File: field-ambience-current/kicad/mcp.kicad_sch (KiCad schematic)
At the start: 68 parts, among them SW10 Modifier CLEAR (12x12x7.3 SMD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, SW6 Modifier SHIFT (12x12x7.3 SMD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, SW7 Modifier HOLD (12x12x7.3 SMD-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, SW8 Modifier DRONE (12x12x7.3 SMD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, SW9 Modifier GENERATE (12x12x7.3 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, U10 PCA9685PW #2 (16-Ch I²C PWM, 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, U2 MCP23017-E/SS (I/O-Expander), U6 PCA9685PW (16-Ch I²C PWM LED-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

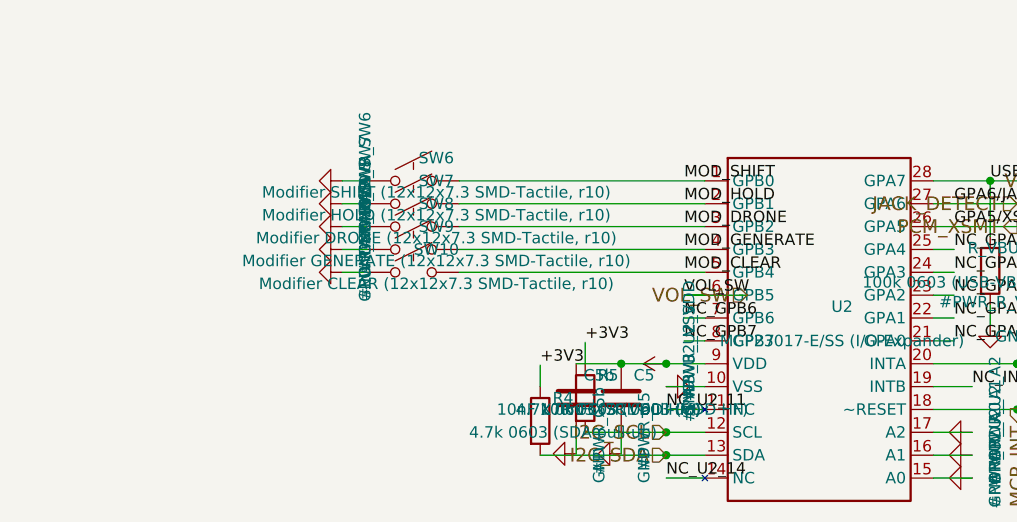
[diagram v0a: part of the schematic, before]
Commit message: parts: resolve ECO items — MIDI LCSC, button SMD→THT, TPS22918 LCSC, pinmap (#79)
* docs(pcb): completeness package — pinmap, JLC BOM export, handoff doc

Make the PCB design data component- and connectivity-complete so a PCB
engineer knows every pin / net / module without re-deriving from the
generator. Closes the gaps from the hardware gap analysis: the BOM alone
isn't production-ready, the generator is the source of truth, and the
pinmap / machine BOM / handoff package were missing.

New deliverables:
- docs/hardware/PINMAP.md — every STM32H743 LQFP-100 pin (all 100) → net →
  function/AF → module → external-component pin, plus per-module net tables
  (source → all sinks) for Power/MCU/LCD/MCP+LEDs/Encoders/Audio/Battery,
  and the verified free-pin list. Distilled from the generator NETS table.
- kicad/export_jlc_bom.py — stdlib-only JLC BOM exporter; parses the 7
  generated leaf .kicad_sch, skips #PWR + DNP, groups by LCSC, quotes
  comma-bearing values. Parts without LCSC go to a stderr NO-LCSC list
  (no guessing). Prints that CPL needs a routed .kicad_pcb (doesn't exist).
- kicad/jlc_bom.csv — generated: 57 LCSC parts, 188 placements.
- docs/hardware/PCB_HANDOFF.md — what's in the package, the engineer
  workflow, and the hard blockers before a fab order (ERC in GUI, layout +
  routing, mechanical coords, Gerber/CPL — all KiCad-GUI / user-side since
  there is no kicad-cli in this env).

Generator: swap LED6/LED7 physical colors to spec — Shift = gelb (C2287),
Hold = gruen (C12624) — attribute-only (same footprint/pads/net), so the
schematic, BOM and firmware are now consistent. Regenerated mcp.kicad_sch.

Also: PROJECT_STATUS r18.64 (1.9" display freeze, per-world musical
identity, Echo/Blur); MECHANICAL_REQUIREMENTS 1.9" freeze line;
component_reviews/README F-1/F-2/F-3 status corrections.

Docs/kicad/tools only — outside the firmware CI path filter.

Co-Authored-By: Claude Opus 4.8 <noreply@anthropic.com>
Claude-Session: https://claude.ai/code/session_01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
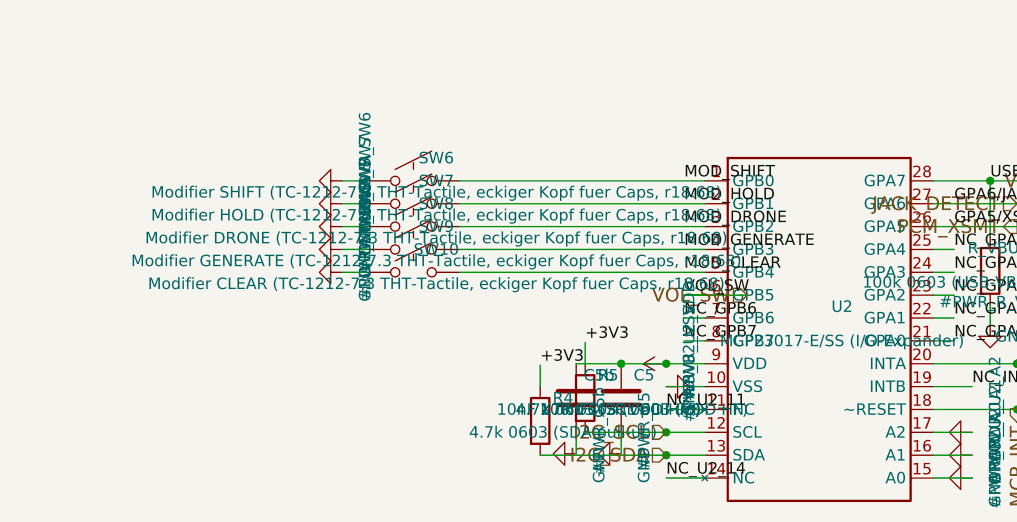
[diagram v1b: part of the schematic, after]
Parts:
- SW10: value Modifier CLEAR (12x12x7.3 SMD-Tactile, r10) -> Modifier CLEAR (TC-1212-7.3 THT-Tactile, eckiger Kopf fuer Caps, r18.68); footprint field_ambience:SW_HX_12x12x7.3_SMD-4P -> field_ambience:SW_TC1212-7.3_THT_4P; FP_NOTE Custom-Footprint libraries/field_ambience.pretty/SW_HX_12x1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 -> field_ambience:SW_TC1212-7.3_THT_4P (easyeda2kicad C2845240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; LCSC C36498966 -> C2845240; MPN HX 12x12x7.3TPFT-B -> TC-1212-7.3-260G; Manufacturer hanxia -> HCTL; Package SMD-4P 11.8x11.8mm, vertical tactile, 7.3mm height, SPST 25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 -> THT 4-pin 11.8x11.8mm, square-head plunger 7.3mm (clip-on c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
- SW6: value Modifier SHIFT (12x12x7.3 SMD-Tactile, r10) -> Modifier SHIFT (TC-1212-7.3 THT-Tactile, eckiger Kopf fuer Caps, r18.68); footprint field_ambience:SW_HX_12x12x7.3_SMD-4P -> field_ambience:SW_TC1212-7.3_THT_4P; FP_NOTE Custom-Footprint libraries/field_ambience.pretty/SW_HX_12x1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 -> field_ambience:SW_TC1212-7.3_THT_4P (easyeda2kicad C2845240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; LCSC C36498966 -> C2845240; MPN HX 12x12x7.3TPFT-B -> TC-1212-7.3-260G; Manufacturer hanxia -> HCTL; Package SMD-4P 11.8x11.8mm, vertical tactile, 7.3mm height, SPST 25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 -> THT 4-pin 11.8x11.8mm, square-head plunger 7.3mm (clip-on c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
- SW7: value Modifier HOLD (12x12x7.3 SMD-Tactile, r10) -> Modifier HOLD (TC-1212-7.3 THT-Tactile, eckiger Kopf fuer Caps, r18.68); footprint field_ambience:SW_HX_12x12x7.3_SMD-4P -> field_ambience:SW_TC1212-7.3_THT_4P; FP_NOTE Custom-Footprint libraries/field_ambience.pretty/SW_HX_12x1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 -> field_ambience:SW_TC1212-7.3_THT_4P (easyeda2kicad C2845240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; LCSC C36498966 -> C2845240; MPN HX 12x12x7.3TPFT-B -> TC-1212-7.3-260G; Manufacturer hanxia -> HCTL; Package SMD-4P 11.8x11.8mm, vertical tactile, 7.3mm height, SPST 25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 -> THT 4-pin 11.8x11.8mm, square-head plunger 7.3mm (clip-on c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
- SW8: value Modifier DRONE (12x12x7.3 SMD-Tactile, r10) -> Modifier DRONE (TC-1212-7.3 THT-Tactile, eckiger Kopf fuer Caps, r18.68); footprint field_ambience:SW_HX_12x12x7.3_SMD-4P -> field_ambience:SW_TC1212-7.3_THT_4P; FP_NOTE Custom-Footprint libraries/field_ambience.pretty/SW_HX_12x1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 -> field_ambience:SW_TC1212-7.3_THT_4P (easyeda2kicad C2845240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; LCSC C36498966 -> C2845240; MPN HX 12x12x7.3TPFT-B -> TC-1212-7.3-260G; Manufacturer hanxia -> HCTL; Package SMD-4P 11.8x11.8mm, vertical tactile, 7.3mm height, SPST 25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 -> THT 4-pin 11.8x11.8mm, square-head plunger 7.3mm (clip-on c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
- SW9: value Modifier GENERATE (12x12x7.3 SMD-Tactile, r10) -> Modifier GENERATE (TC-1212-7.3 THT-Tactile, eckiger Kopf fuer Caps, r18.68); footprint field_ambience:SW_HX_12x12x7.3_SMD-4P -> field_ambience:SW_TC1212-7.3_THT_4P; FP_NOTE Custom-Footprint libraries/field_ambience.pretty/SW_HX_12x1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 -> field_ambience:SW_TC1212-7.3_THT_4P (easyeda2kicad C2845240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; LCSC C36498966 -> C2845240; MPN HX 12x12x7.3TPFT-B -> TC-1212-7.3-260G; Manufacturer hanxia -> HCTL; Package SMD-4P 11.8x11.8mm, vertical tactile, 7.3mm height, SPST 25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 -> THT 4-pin 11.8x11.8mm, square-head plunger 7.3mm (clip-on c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

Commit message: kicad(gen): flow the 5 sourcing-fix part swaps into the generator (r18.71)
The generator is the schematic's source of truth, so the BOM part swaps must
live here (previously only in BOM/HTML). Swapped LCSC + MPN in the generator,
regenerated the .kicad_sch, re-exported jlc_bom.csv:
- FB2 ferrite C84094 -> C19330 (same Murata MPN, JLC 950k)
- VCAP C24539 -> C23630 (2.2uF 16V X5R 0603, JLC Basic)
- charger LED C72041 (blue+EOL!) -> C965800 (orange 605nm 0603)
- C_BULK2 C2880380 (stock 1) -> C23742 (100uF 10V X5R 1210)
- modifier buttons SW6-10 C2845240 (stock 30) -> C36498965 (HX B3F square
  head); footprint SW_TC1212-7.3_THT_4P reused, HX pinout verify noted in FP_NOTE.

The generated schematic Aron opens now carries the correct in-stock parts.
check_pinmap passes; jlc_bom.csv has the new codes (old ones gone).

Co-Authored-By: Claude Opus 4.8 <noreply@anthropic.com>
Claude-Session: https://claude.ai/code/session_01K5kLTFpDCCoYwx2dq6RkAv
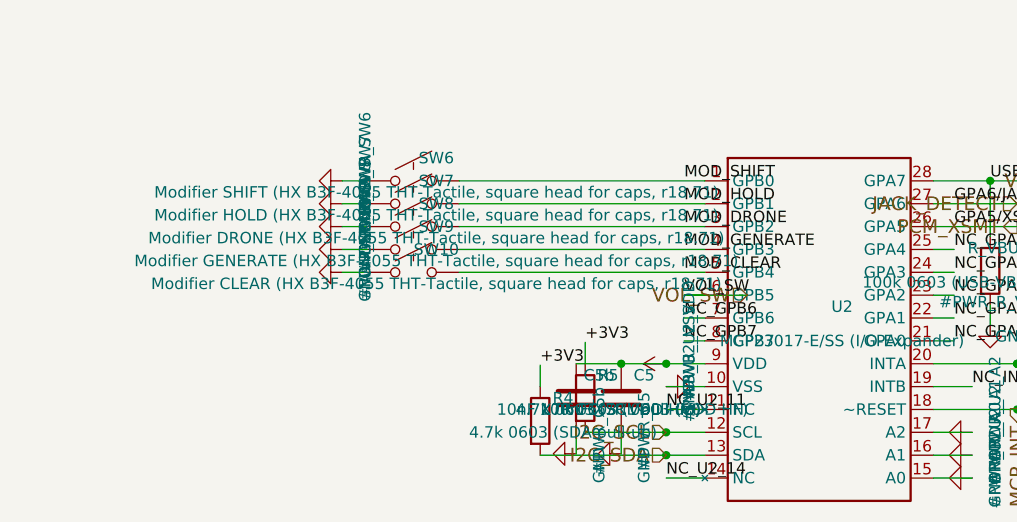
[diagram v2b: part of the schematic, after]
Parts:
- SW10: value Modifier CLEAR (TC-1212-7.3 THT-Tactile, eckiger Kopf fuer Caps, r18.68) -> Modifier CLEAR (HX B3F-4055 THT-Tactile, square head for caps, r18.71); FP_NOTE field_ambience:SW_TC1212-7.3_THT_4P (easyeda2kicad C2845240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 -> r18.71: was TC-1212-7.3-260G C2845240 (JLC stock 30); -> HX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; LCSC C2845240 -> C36498965; MPN TC-1212-7.3-260G -> HX B3F-4055-Y; Manufacturer HCTL -> HX; Package THT 4-pin 11.8x11.8mm, square-head plunger 7.3mm (clip-on caps), SPST 2.6N, 100k cycles, 12V/50mA -> THT 4-pin 11.8x11.8mm, square-head plunger 7.3mm (clip-on caps), SPST 2.5N, 100k cycles, 12V/50mA
- SW6: value Modifier SHIFT (TC-1212-7.3 THT-Tactile, eckiger Kopf fuer Caps, r18.68) -> Modifier SHIFT (HX B3F-4055 THT-Tactile, square head for caps, r18.71); FP_NOTE field_ambience:SW_TC1212-7.3_THT_4P (easyeda2kicad C2845240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 -> r18.71: was TC-1212-7.3-260G C2845240 (JLC stock 30); -> HX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; LCSC C2845240 -> C36498965; MPN TC-1212-7.3-260G -> HX B3F-4055-Y; Manufacturer HCTL -> HX; Package THT 4-pin 11.8x11.8mm, square-head plunger 7.3mm (clip-on caps), SPST 2.6N, 100k cycles, 12V/50mA -> THT 4-pin 11.8x11.8mm, square-head plunger 7.3mm (clip-on caps), SPST 2.5N, 100k cycles, 12V/50mA
- SW7: value Modifier HOLD (TC-1212-7.3 THT-Tactile, eckiger Kopf fuer Caps, r18.68) -> Modifier HOLD (HX B3F-4055 THT-Tactile, square head for caps, r18.71); FP_NOTE field_ambience:SW_TC1212-7.3_THT_4P (easyeda2kicad C2845240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 -> r18.71: was TC-1212-7.3-260G C2845240 (JLC stock 30); -> HX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; LCSC C2845240 -> C36498965; MPN TC-1212-7.3-260G -> HX B3F-4055-Y; Manufacturer HCTL -> HX; Package THT 4-pin 11.8x11.8mm, square-head plunger 7.3mm (clip-on caps), SPST 2.6N, 100k cycles, 12V/50mA -> THT 4-pin 11.8x11.8mm, square-head plunger 7.3mm (clip-on caps), SPST 2.5N, 100k cycles, 12V/50mA
- SW8: value Modifier DRONE (TC-1212-7.3 THT-Tactile, eckiger Kopf fuer Caps, r18.68) -> Modifier DRONE (HX B3F-4055 THT-Tactile, square head for caps, r18.71); FP_NOTE field_ambience:SW_TC1212-7.3_THT_4P (easyeda2kicad C2845240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 -> r18.71: was TC-1212-7.3-260G C2845240 (JLC stock 30); -> HX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; LCSC C2845240 -> C36498965; MPN TC-1212-7.3-260G -> HX B3F-4055-Y; Manufacturer HCTL -> HX; Package THT 4-pin 11.8x11.8mm, square-head plunger 7.3mm (clip-on caps), SPST 2.6N, 100k cycles, 12V/50mA -> THT 4-pin 11.8x11.8mm, square-head plunger 7.3mm (clip-on caps), SPST 2.5N, 100k cycles, 12V/50mA
- SW9: value Modifier GENERATE (TC-1212-7.3 THT-Tactile, eckiger Kopf fuer Caps, r18.68) -> Modifier GENERATE (HX B3F-4055 THT-Tactile, square head for caps, r18.71); FP_NOTE field_ambience:SW_TC1212-7.3_THT_4P (easyeda2kicad C2845240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 -> r18.71: was TC-1212-7.3-260G C2845240 (JLC stock 30); -> HX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; LCSC C2845240 -> C36498965; MPN TC-1212-7.3-260G -> HX B3F-4055-Y; Manufacturer HCTL -> HX; Package THT 4-pin 11.8x11.8mm, square-head plunger 7.3mm (clip-on caps), SPST 2.6N, 100k cycles, 12V/50mA -> THT 4-pin 11.8x11.8mm, square-head plunger 7.3mm (clip-on caps), SPST 2.5N, 100k cycles, 12V/50mA

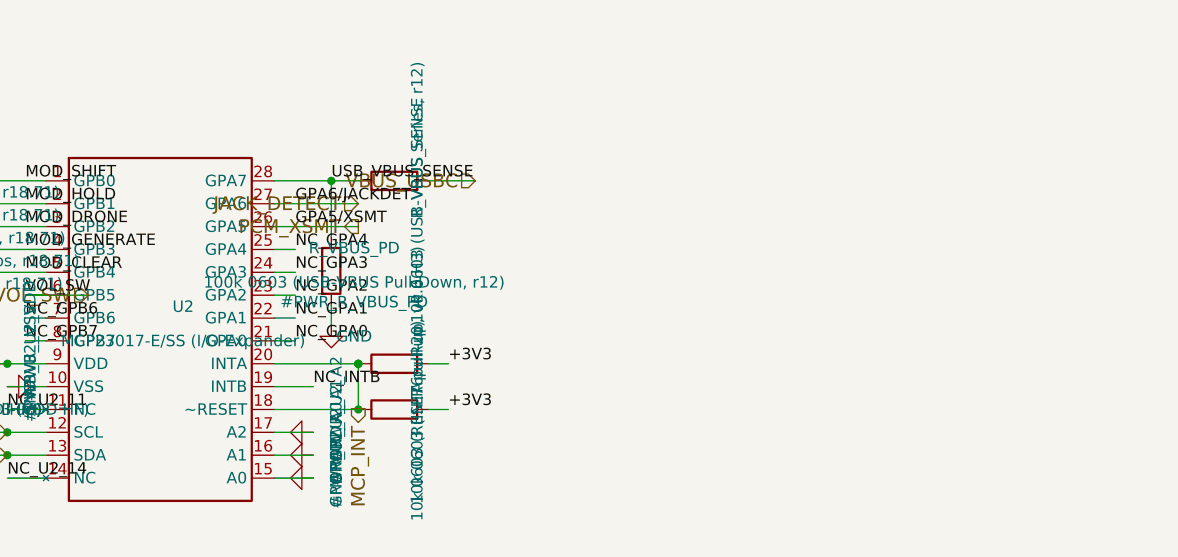
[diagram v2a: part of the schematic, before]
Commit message: cells: Hall/ADC → digital I²C switches on MCP23017 (ADR-0013 superseded, r18.73) (#85)
Per user direction (HiChord Batch 4+ reference): the 5 cells change from
Gateron-magnetic + DRV5056A4 Hall (analog velocity at the STM32 ADC) to plain
digital on/off tactile switches on the existing MCP23017 I²C expander — the
HiChord Batch 4+ topology (switch → I²C GPIO-expander → MCU).

No new component: SW1–SW5 reuse the same already-verified HX B3F-4055-Y
(LCSC C36498965) part as the modifier buttons SW6–SW10, on the already-free
expander pins GPA0–GPA4 (nets CELL1..5_BTN). This restores the original
SPEC v0.6 §7 "10 switches" topology (5 cells + 5 modifiers on the expander).

Generator (generate_kicad_project.py):
- mcp_sheet: NC_GPA0..4 placeholders → SW1–SW5 cell switches on GPA0–GPA4,
  mirroring the SW6–SW10 modifier wiring (pin → GND, MCP pull-up, shared INT).
- stm32 sheet: removed 5× DRV5056A4 (J_CELL1–5), 5× R_CELL 1k, 5× C_CELL 10nF;
  freed the 5 ADC pins PC0/PC1/PA4/PB0/PB1 as NC reserves (Rev-B option).
- Regenerated schematics, jlc_bom.csv (56 LCSC parts; DRV5056A4 gone, SW1–SW10
  all C36498965), and Aron's bom_overview.html.

Docs updated to match: BOM_MASTER §7, PCB_BOM, PINMAP, KICAD_BLUEPRINT,
SCHEMATIC_WALKTHROUGH, MECHANICAL_REQUIREMENTS, PCB_FOOTPRINT_RISK_AUDIT,
field_ambience_pcb_SPEC_v0.7 §5.6a, ADR-0013 (SUPERSEDED banner), ADR-0016
(Hall-current premise amended), mechanical_coordinates, PROJECT_QUALITY,
PROJECT_STATUS, CHANGELOG, COST_ESTIMATE. Hall kept as the documented option
only if expressive press-depth/velocity is wanted later.

Host tests green (352298 checks, 0 failures); firmware untouched.


Claude-Session: https://claude.ai/code/session_019pKguH6aG4iazMCWJnpmMn

Co-authored-by: Claude <noreply@anthropic.com>
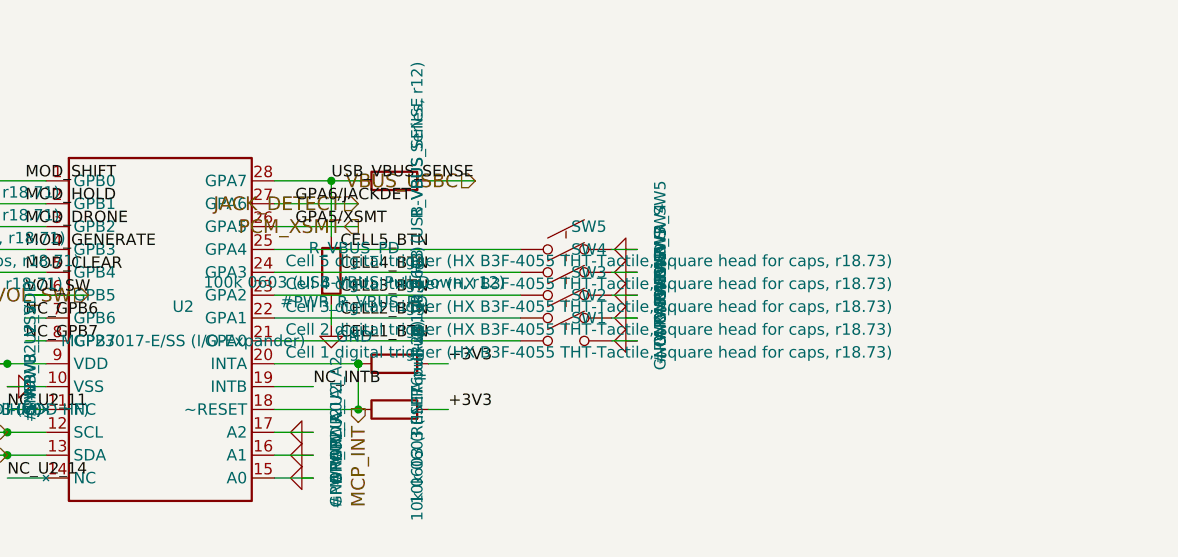
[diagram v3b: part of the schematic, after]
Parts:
- added SW1: Cell 1 digital trigger (HX B3F-4055 THT-Tactile, 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, field_ambience:SW_TC1212-7.3_THT_4P, symbol Switch:SW_Push
- added SW2: Cell 2 digital trigger (HX B3F-4055 THT-Tactile, 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, field_ambience:SW_TC1212-7.3_THT_4P, symbol Switch:SW_Push
- added SW3: Cell 3 digital trigger (HX B3F-4055 THT-Tactile, 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, field_ambience:SW_TC1212-7.3_THT_4P, symbol Switch:SW_Push
- added SW4: Cell 4 digital trigger (HX B3F-4055 THT-Tactile, 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, field_ambience:SW_TC1212-7.3_THT_4P, symbol Switch:SW_Push
- added SW5: Cell 5 digital trigger (HX B3F-4055 THT-Tactile, 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, field_ambience:SW_TC1212-7.3_THT_4P, symbol Switch:SW_Push
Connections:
- net GND: now also SW1.2, SW2.2, SW3.2, SW4.2, SW5.2
- net NC_GPA0 renamed CELL1_BTN
- net CELL1_BTN: now also SW1.1
- net NC_GPA1 renamed CELL2_BTN
- net CELL2_BTN: now also SW2.1
- net NC_GPA2 renamed CELL3_BTN
- net CELL3_BTN: now also SW3.1
- net NC_GPA3 renamed CELL4_BTN
- net CELL4_BTN: now also SW4.1
- net NC_GPA4 renamed CELL5_BTN
- net CELL5_BTN: now also SW5.1
